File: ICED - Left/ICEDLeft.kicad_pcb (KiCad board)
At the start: 2 copper layers, 175.4 x 145 mm, 164 parts, among them P1 FLASH_HDR, P2 USBC, P3 CONN_17, P4 USB3_AFEMALE, Q1 TC1264, U1 MK20DX256VLH7, U2 IS31FL3731C, X1 CRYSTAL

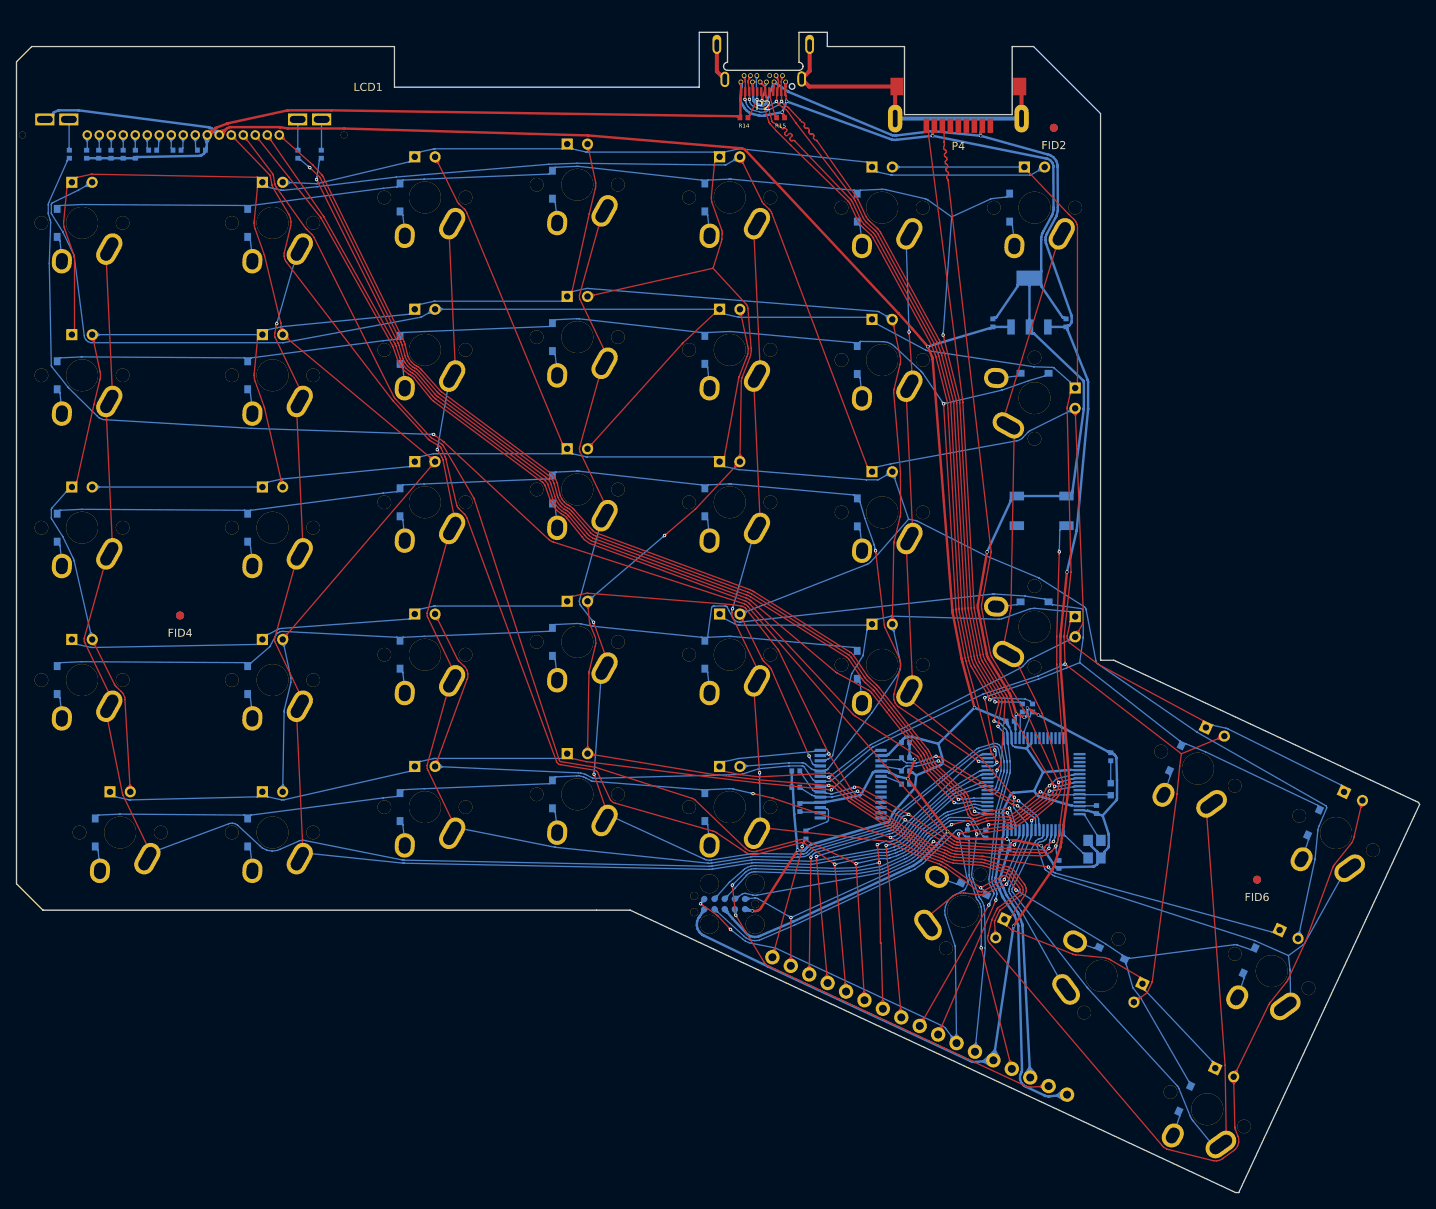
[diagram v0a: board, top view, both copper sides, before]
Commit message: Finished laying out components
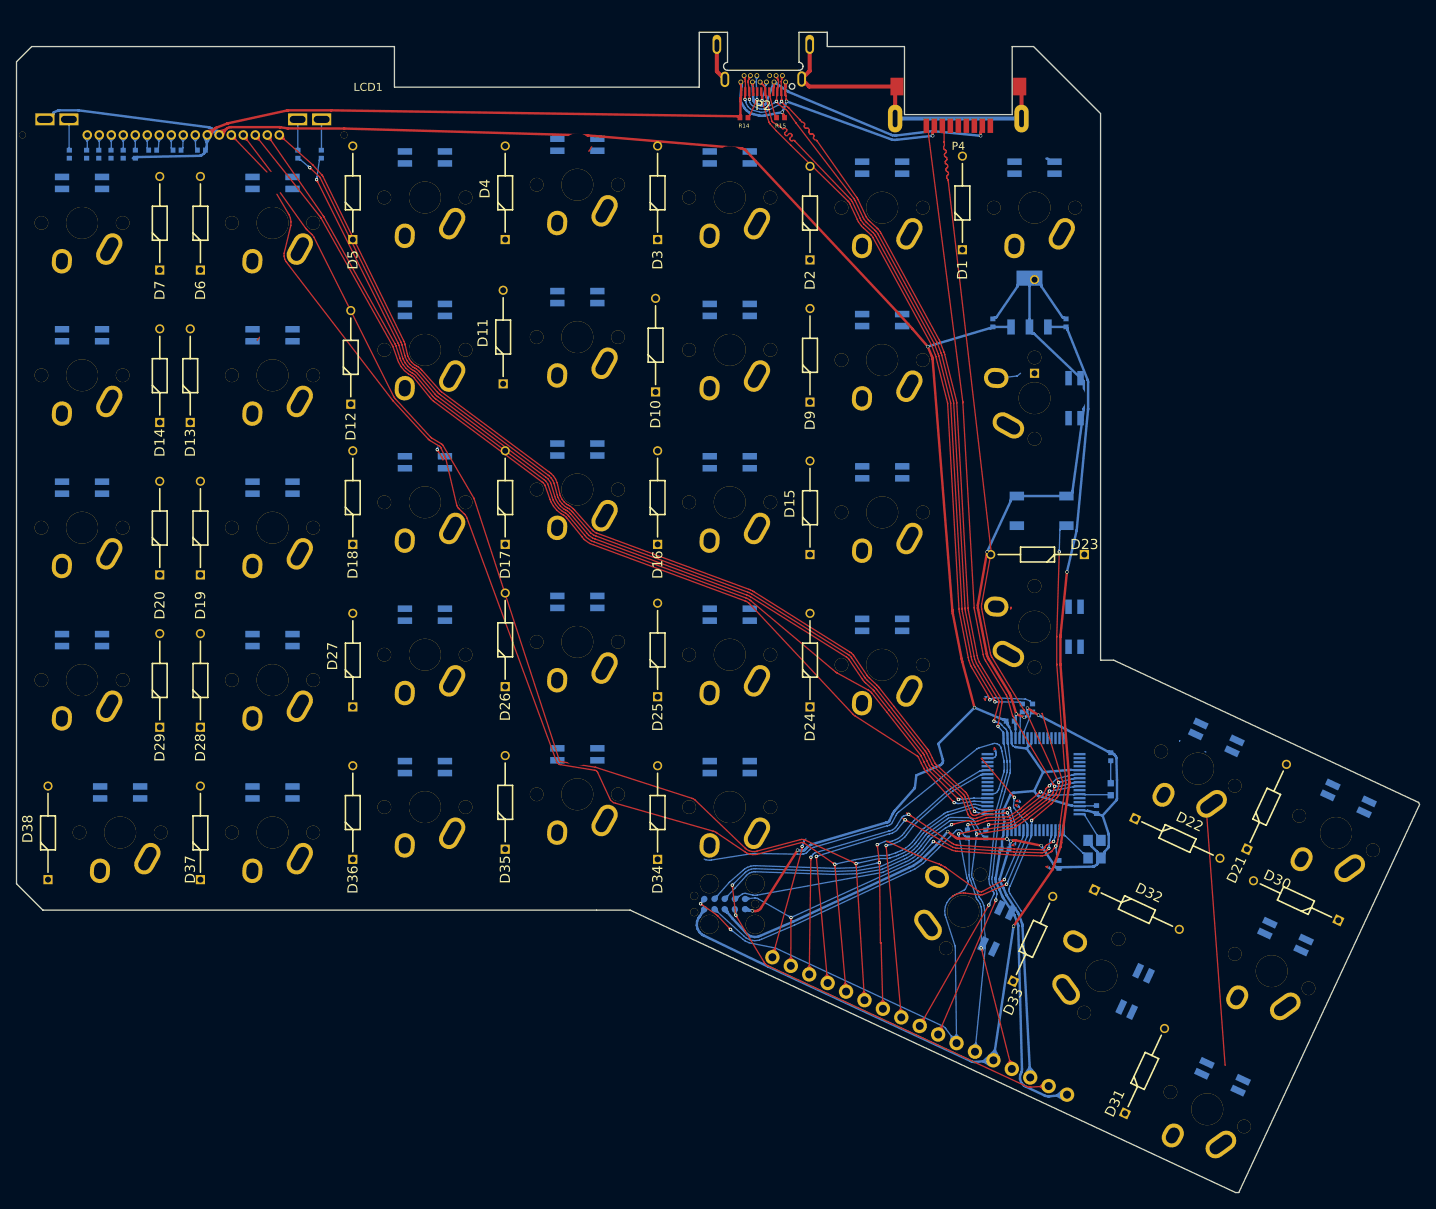
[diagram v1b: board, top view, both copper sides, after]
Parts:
- removed C6: 1uF, prettylib:SMD-1005
- removed C8: 0.22uF, prettylib:SMD-1005
- removed C9: 0.1uF, prettylib:SMD-1005
- removed D39, D40, D41, D42, D43, D44, D45, D46, D47, D48, D49, D50, D51, D52, D53, D54, D55, D56, D57, D58, D59, D60, D61, D62, D63, D64, D65, D66, D67, D68, D69, D70, D71, D72, D73, D74, D75, D76: LED, prettylib:INSW_LEDS_REG
- removed FID1, FID2, FID3, FID4, FID5, FID6: >VALUE, prettylib:FID
- removed IC_LOGO: , prettylib:IC_LOGO
- removed R12: 20k, prettylib:SMD-1005
- removed R3, R4, R5: 4.7k, prettylib:SMD-1005
- removed R8: 100k, prettylib:SMD-1005
- removed U2: IS31FL3731C, prettylib:SSOP-28
- added LED1: SK6812MINI-E, prettylib:SK6812MINIE, B.Cu at (144.9, 42.7)
- added LED10: SK6812MINI-E, prettylib:SK6812MINIE, B.Cu at (106.8, 60.5)
- added LED11: SK6812MINI-E, prettylib:SK6812MINIE, B.Cu at (87.8, 58.9)
- added LED12: SK6812MINI-E, prettylib:SK6812MINIE, B.Cu at (68.7, 60.5)
- added LED13: SK6812MINI-E, prettylib:SK6812MINIE, B.Cu at (49.7, 63.7)
- added LED14: SK6812MINI-E, prettylib:SK6812MINIE, B.Cu at (25.8, 63.7)
- added LED15: SK6812MINI-E, prettylib:SK6812MINIE, B.Cu at (125.9, 80.8)
- added LED16: SK6812MINI-E, prettylib:SK6812MINIE, B.Cu at (106.8, 79.5)
- added LED17: SK6812MINI-E, prettylib:SK6812MINIE, B.Cu at (87.8, 77.9)
- added LED18: SK6812MINI-E, prettylib:SK6812MINIE, B.Cu at (68.7, 79.5)
- added LED19: SK6812MINI-E, prettylib:SK6812MINIE, B.Cu at (49.7, 82.7)
- added LED2: SK6812MINI-E, prettylib:SK6812MINIE, B.Cu at (125.9, 42.7)
- added LED20: SK6812MINI-E, prettylib:SK6812MINIE, B.Cu at (25.8, 82.7)
- added LED21: SK6812MINI-E, prettylib:SK6812MINIE, B.Cu at (184.2, 121.5)
- added LED22: SK6812MINI-E, prettylib:SK6812MINIE, B.Cu at (167.6, 113.9)
- added LED23: SK6812MINI-E, prettylib:SK6812MINIE, B.Cu at (149.9, 100.1)
- added LED24: SK6812MINI-E, prettylib:SK6812MINIE, B.Cu at (125.9, 99.8)
- added LED25: SK6812MINI-E, prettylib:SK6812MINIE, B.Cu at (106.8, 98.6)
- added LED26: SK6812MINI-E, prettylib:SK6812MINIE, B.Cu at (87.8, 97.0)
- added LED27: SK6812MINI-E, prettylib:SK6812MINIE, B.Cu at (68.7, 98.6)
- added LED28: SK6812MINI-E, prettylib:SK6812MINIE, B.Cu at (49.7, 101.8)
- added LED29: SK6812MINI-E, prettylib:SK6812MINIE, B.Cu at (25.8, 101.8)
- added LED3: SK6812MINI-E, prettylib:SK6812MINIE, B.Cu at (106.8, 41.4)
- added LED30: SK6812MINI-E, prettylib:SK6812MINIE, B.Cu at (176.3, 138.8)
- added LED31: SK6812MINI-E, prettylib:SK6812MINIE, B.Cu at (168.4, 156.3)
- added LED32: SK6812MINI-E, prettylib:SK6812MINIE, B.Cu at (157.5, 145.7)
- added LED33: SK6812MINI-E, prettylib:SK6812MINIE, B.Cu at (140.2, 137.8)
- added LED34: SK6812MINI-E, prettylib:SK6812MINIE, B.Cu at (106.8, 117.6)
- added LED35: SK6812MINI-E, prettylib:SK6812MINIE, B.Cu at (87.8, 116.0)
- added LED36: SK6812MINI-E, prettylib:SK6812MINIE, B.Cu at (68.7, 117.6)
- added LED37: SK6812MINI-E, prettylib:SK6812MINIE, B.Cu at (49.7, 120.8)
- added LED38: SK6812MINI-E, prettylib:SK6812MINIE, B.Cu at (30.6, 120.8)
- added LED4: SK6812MINI-E, prettylib:SK6812MINIE, B.Cu at (87.8, 39.8)
- added LED5: SK6812MINI-E, prettylib:SK6812MINIE, B.Cu at (68.7, 41.4)
- added LED6: SK6812MINI-E, prettylib:SK6812MINIE, B.Cu at (49.7, 44.6)
- added LED7: SK6812MINI-E, prettylib:SK6812MINIE, B.Cu at (25.8, 44.6)
- added LED8: SK6812MINI-E, prettylib:SK6812MINIE, B.Cu at (149.9, 71.5)
- added LED9: SK6812MINI-E, prettylib:SK6812MINIE, B.Cu at (125.9, 61.7)
- D1, D10, D11, D12, D13, D14, D15, D16, D17, D18, D19, D2, D20, D21, D22, D23, D24, D25, D26, D27, D28, D29, D3, D30, D31, D32, D33, D34, D35, D36, D37, D38, D4, D5, D6, D7, D9: footprint prettylib:SOT123-DIODE -> prettylib:1N4148; moved to F.Cu
- D8: footprint prettylib:SOT123-DIODE -> prettylib:1N4148
- moved D14 14.1 mm to (35.6, 74.5), turned to 90 degrees
- moved D20 14.1 mm to (35.6, 93.6), turned to 90 degrees
- moved D29 14.1 mm to (35.6, 112.6), turned to 90 degrees
- moved D7 14.1 mm to (35.6, 55.5), turned to 90 degrees
- moved D33 12.6 mm to (142.2, 144.4)
- moved D30 12.2 mm to (182.9, 136.8)
- moved D13 9.29 mm to (39.4, 74.5), turned to 90 degrees
- moved D12 9.16 mm to (59.4, 72.3), turned to 90 degrees
- moved D22 9.09 mm to (157.5, 124.1), turned to 335 degrees
- moved D17 9.05 mm to (78.7, 89.8), turned to 90 degrees
- moved D4 9.05 mm to (78.7, 51.7), turned to 90 degrees
- moved D35 9.05 mm to (78.7, 127.9), turned to 90 degrees
- moved D21 8.97 mm to (171.4, 127.9), turned to 65 degrees
- moved D34 8.80 mm to (97.8, 129.2), turned to 90 degrees
- moved D27 8.80 mm to (59.7, 110.1), turned to 90 degrees
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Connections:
- C14 pad 1: VSS -> (no net)
- C15 pad 1: VSS -> (no net)
- C16 pad 1: VSS -> (no net)
- C17 pad 1: VSS -> (no net)
- P2 pad 20: Net-(P2-Pad20) -> (no net)
- P2 pad 8: Net-(P2-Pad8) -> (no net)
- P3 pad 17: /mcu/AUD -> (no net)
- P4 pad 2: Net-(P4-Pad2) -> (no net)
- P4 pad 3: Net-(P4-Pad3) -> (no net)
- P4 pad 7: Net-(P4-Pad7) -> (no net)
- P4 pad 8: Net-(P4-Pad8) -> (no net)
- P4 pad 9: Net-(P4-Pad9) -> (no net)
- S19 pad 1: /Col8 -> (no net)
- S25 pad 1: /Col5 -> (no net)
- S26 pad 1: /Col6 -> (no net)
- S31 pad 1: /Col2 -> (no net)
- S39 pad 1: Net-(S39-Pad1) -> (no net)
- U1 pad 10: /mcu/ADC0_DM0 -> /GND
- U1 pad 11: /mcu/ADC1_DP0 -> (no net)
- U1 pad 12: /mcu/ADC1_DM0 -> (no net)
- U1 pad 13: Net-(U1-Pad13) -> (no net)
- U1 pad 14: Net-(U1-Pad14) -> (no net)
- U1 pad 15: Net-(U1-Pad15) -> (no net)
- U1 pad 16: Net-(U1-Pad16) -> (no net)
- U1 pad 17: Net-(U1-Pad17) -> (no net)
- U1 pad 18: Net-(U1-Pad18) -> (no net)
- U1 pad 19: Net-(U1-Pad19) -> (no net)
- U1 pad 20: Net-(U1-Pad20) -> (no net)
- U1 pad 26: /mcu/PTA4 -> (no net)
- U1 pad 28: /mcu/PTA12 -> (no net)
- U1 pad 29: /mcu/PTA13 -> (no net)
- U1 pad 39: /mcu/SDB -> (no net)
- U1 pad 40: /mcu/INTB -> (no net)
- U1 pad 9: /mcu/ADC0_DP0 -> (no net)
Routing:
- net /ledmatrix/CA2: track 431.6 -> 0.00 mm, vias 1 -> 0
- net /ledmatrix/CA3: track 389.0 -> 0.00 mm, vias 1 -> 0
- net /ledmatrix/CA1: track 376.8 -> 0.00 mm, vias 2 -> 0
- net /ledmatrix/CA5: track 309.3 -> 0.00 mm, vias 1 -> 0
- net /ledmatrix/CA4: track 288.6 -> 1.26 mm
- net /Row4: track 222.4 -> 3.76 mm, vias 2 -> 0
- net /Row1: track 197.8 -> 0.00 mm, vias 2 -> 0
- net /Row5: track 194.4 -> 0.00 mm, vias 4 -> 0
- net /Col9: track 190.3 -> 0.83 mm
- net /Row2: track 180.5 -> 0.00 mm, vias 2 -> 0
- net /ledmatrix/CA7: track 174.1 -> 1.11 mm, vias 2 -> 0
- net /mcu/LCD_KR: track 174.0 -> 1.11 mm, vias 2 -> 0
- net /Col8: track 170.1 -> 0.00 mm, vias 1 -> 0
- net /Col7: track 160.8 -> 3.44 mm
- net /Row3: track 145.1 -> 0.00 mm, vias 2 -> 0
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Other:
- board text added: "Ergodox Aleph v0.1 by @stillinbeta"
- board text removed: "ICED-L Rev 1.2b Batch __"

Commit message: routed and DRC'd
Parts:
- moved D30 18.3 mm to (173.4, 152.5)
- moved D8 13.5 mm to (139.2, 80.6), turned to 0 degrees
- moved D23 11.2 mm to (140.0, 90.5), turned to 0 degrees
- moved D34 3.21 mm to (97.8, 125.9)
- moved D13 2.60 mm to (40.6, 72.3)
- moved D17 2.54 mm to (78.7, 87.2)
- moved D14 2.34 mm to (35.1, 72.3)
- moved D29 2.30 mm to (35.3, 110.4)
- moved D35 2.30 mm to (78.5, 125.6)
- moved D28 2.29 mm to (40.6, 110.4)
- moved D4 1.96 mm to (78.2, 49.8)
- moved D19 1.78 mm to (40.6, 91.8)
- moved D20 1.78 mm to (35.6, 91.8)
- moved D15 1.61 mm to (117.3, 89.5)
- moved D37 1.60 mm to (40.6, 130.1)
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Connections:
- C14 pad 1: (no net) -> VSS
- C15 pad 1: (no net) -> VSS
- C16 pad 1: (no net) -> VSS
- C17 pad 1: (no net) -> VSS
- S19 pad 1: (no net) -> /Col8
- S25 pad 1: (no net) -> /Col5
- S26 pad 1: (no net) -> /Col6
- S31 pad 1: (no net) -> /Col2
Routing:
- net VSS: track 332.9 -> 1170.4 mm, vias 12 -> 25
- net VDD: track 307.7 -> 974.2 mm, vias 4 -> 15
- net /Row4: track 3.76 -> 213.7 mm, vias 0 -> 3
- net /mcu/LCD_KR: track 1.11 -> 205.3 mm, vias 0 -> 2
- net /Row1: track 0.00 -> 198.8 mm, vias 0 -> 1
- net /Row2: track 0.00 -> 194.8 mm, vias 0 -> 2
- net /Row5: track 0.00 -> 194.4 mm, vias 0 -> 5
- net /Col9: track 0.83 -> 189.3 mm, vias 0 -> 1
- net /Col8: track 0.00 -> 166.8 mm, vias 0 -> 1
- net /Col7: track 3.44 -> 146.8 mm
- net /Row3: track 0.00 -> 140.7 mm, vias 0 -> 1
- net /GND: track 45.5 -> 149.8 mm, vias 0 -> 2
- net /Col5: track 25.4 -> 120.0 mm
- net /Col3: track 29.9 -> 115.4 mm, vias 1 -> 3
- net /Col4: track 27.9 -> 108.9 mm
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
